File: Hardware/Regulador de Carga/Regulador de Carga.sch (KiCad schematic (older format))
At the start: 16 parts, among them K1 DIPxx-1Cxx-51x

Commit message: Regulador de carga
Modifique el circuito regulador de carga para hacerlo mas compacto y con menor consumo.
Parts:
- removed K1: DIPxx-1Cxx-51x, Relay_THT:Relay_SPDT_Finder_36.11, symbol Relay:DIPxx-1Cxx-51x
- removed ZENER1: D_Zener, Diode_THT:D_A-405_P12.70mm_Horizontal, symbol Device:D_Zener
- added D2: D_Zener, symbol Device:D_Zener
- added Q1: 2N3904, Package_TO_SOT_THT:TO-92_Inline, symbol Transistor_BJT:2N3904
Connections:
- wire segments 54 -> 49
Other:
- moved on the sheet: C3, D1, LED1, PANEL1, R2, RV1, op1

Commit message: Agregar huellas faltantes
le agregue las huellas que faltaban al regulador de carga
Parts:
- D2: footprint (none) -> Diode_THT:D_A-405_P12.70mm_Horizontal
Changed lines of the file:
@@
 F 0 "D2" H 3200 3317 50  0000 C CNN
 F 1 "D_Zener" H 3200 3226 50  0000 C CNN
-F 2 "" H 3200 3100 50  0001 C CNN
+F 2 "Diode_THT:D_A-405_P12.70mm_Horizontal" H 3200 3100 50  0001 C CNN
 F 3 "~" H 3200 3100 50  0001 C CNN
 	1    3200 3100

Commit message: regulador de carga (yeti)
es mi primer placa despues de años. ¿esta fachera, no?
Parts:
- added R4: 1K, Resistor_THT:R_Axial_DIN0204_L3.6mm_D1.6mm_P7.62mm_Horizontal, symbol Device:R
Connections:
- net at D2.2 (A): now also R4.1; no longer Q1.2 (B)
- new net: Q1.2 (B), R4.2
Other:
- moved on the sheet: BATin1, BATout1, C1, C2, C3, D1, D2, LED1, LM7805, PANEL1, Q1, R1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

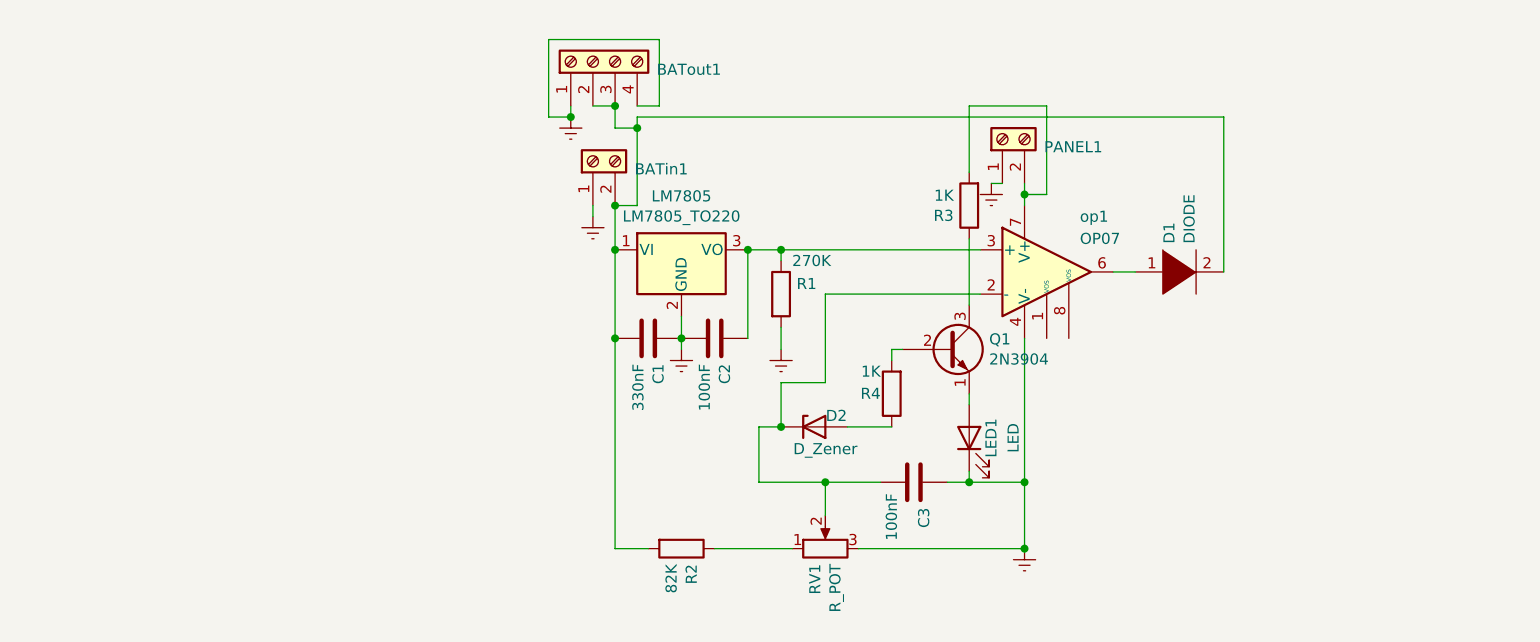
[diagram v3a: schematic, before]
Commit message: Esquematico Regulador de Carga
Agregue los 4 diodos en el esquematico.
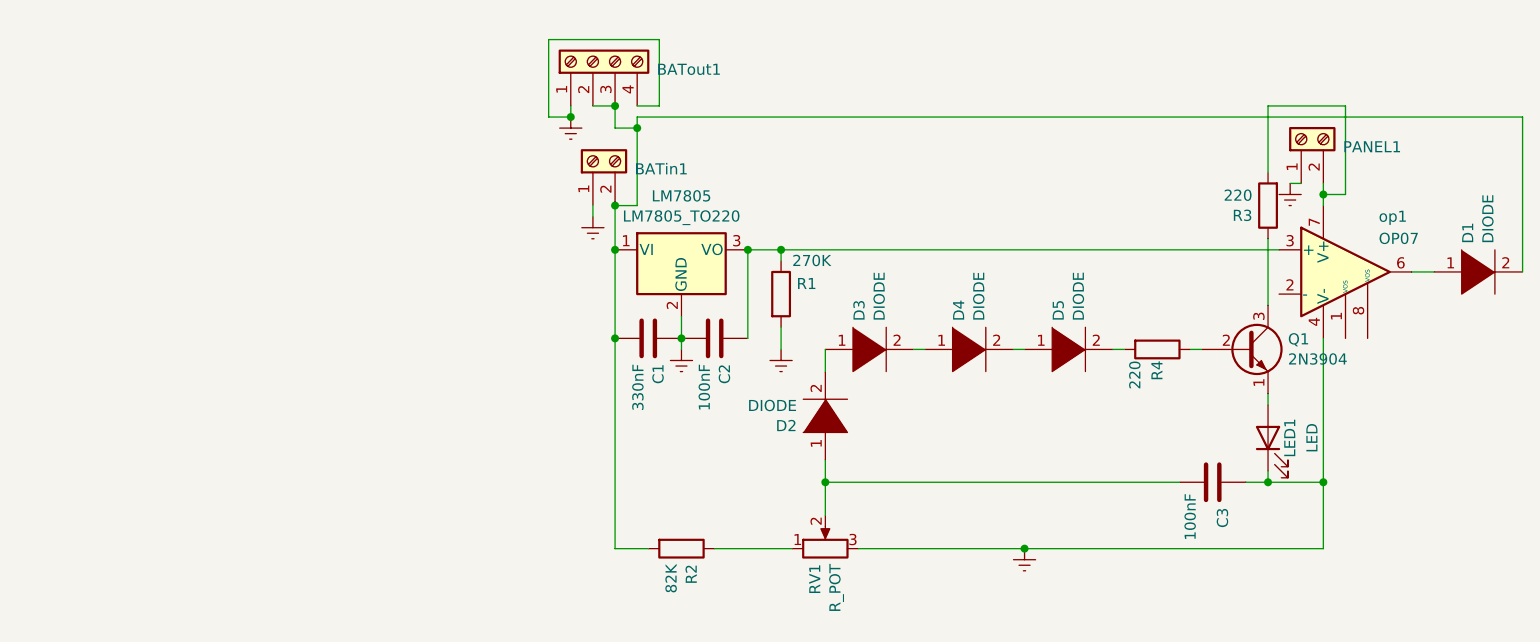
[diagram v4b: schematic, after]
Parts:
- removed D2: D_Zener, Diode_THT:D_A-405_P12.70mm_Horizontal, symbol Device:D_Zener
- added D2, D3, D4, D5: DIODE, Diode_THT:D_A-405_P12.70mm_Horizontal, symbol pspice:DIODE
- R3, R4: value 1K -> 220
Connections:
- net at C3.2, RV1.2: now also D2.1 (K); no longer op1.2 (-)
- net at R4.1: now also Q1.2 (B)
- net at R4.2: now also D5.2 (A); no longer Q1.2 (B)
- new net: D4.2 (A), D5.1 (K)
- new net: D3.2 (A), D4.1 (K)
- new net: D2.2 (A), D3.1 (K)
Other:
- moved on the sheet: C3, D1, LED1, PANEL1, Q1, R3, R4, op1
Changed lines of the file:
@@
 EESchema Schematic File Version 4
-LIBS:Regulador de Carga-cache
-EELAYER 29 0
+EELAYER 30 0
 EELAYER END
 $Descr A4 11693 8268
@@
 L Amplifier_Operational:OP07 op1
 U 1 1 5E9EA082
-P 6450 2850
-F 0 "op1" H 6600 3100 50  0000 L CNN
-F 1 "OP07" H 6600 3000 50  0000 L CNN
-F 2 "Package_DIP:DIP-8_W7.62mm" H 6500 2900 50  0001 C CNN
-F 3 "https://www.analog.com/media/en/technical-documentation/data-sheets/OP07.pdf" H 6500 3000 50  0001 C CNN
-	1    6450 2850
+P 7800 2850
+F 0 "op1" H 7950 3100 50  0000 L CNN
+F 1 "OP07" H 7950 3000 50  0000 L CNN
+F 2 "Package_DIP:DIP-8_W7.62mm" H 7850 2900 50  0001 C CNN
+F 3 "https://www.analog.com/media/en/technical-documentation/data-sheets/OP07.pdf" H 7850 3000 50  0001 C CNN
+	1    7800 2850
 	1    0    0    -1
 $EndComp
@@
 L Device:LED LED1
 U 1 1 5E9EAEE0
-P 6100 3600
-F 0 "LED1" H 6100 3500 50  0000 C CNN
-F 1 "LED" H 6100 3400 50  0000 C CNN
-F 2 "LED_THT:LED_D5.0mm" H 6100 3600 50  0001 C CNN
-F 3 "~" H 6100 3600 50  0001 C CNN
-	1    6100 3600
+P 7450 3600
+F 0 "LED1" H 7450 3500 50  0000 C CNN
+F 1 "LED" H 7450 3400 50  0000 C CNN
+F 2 "LED_THT:LED_D5.0mm" H 7450 3600 50  0001 C CNN
+F 3 "~" H 7450 3600 50  0001 C CNN
+	1    7450 3600
 	0    -1   -1   0
 $EndComp
@@
 L pspice:DIODE D1
 U 1 1 5E9E51EC
-P 7050 2850
-F 0 "D1" V 7004 2978 50  0000 L CNN
-F 1 "DIODE" V 7095 2978 50  0000 L CNN
-F 2 "Diode_THT:D_A-405_P12.70mm_Horizontal" H 7050 2850 50  0001 C CNN
-F 3 "~" H 7050 2850 50  0001 C CNN
-	1    7050 2850
+P 8400 2850
+F 0 "D1" V 8354 2978 50  0000 L CNN
+F 1 "DIODE" V 8445 2978 50  0000 L CNN
+F 2 "Diode_THT:D_A-405_P12.70mm_Horizontal" H 8400 2850 50  0001 C CNN
+F 3 "~" H 8400 2850 50  0001 C CNN
+	1    8400 2850
 	1    0    0    -1
 $EndComp
@@
 Wire Wire Line
 	5250 3100 5250 3200
-Connection ~ 5250 2750
 $Comp
 L Device:C C3
 U 1 1 5E9EDB4A
-P 5850 3800
-F 0 "C3" H 5965 3846 50  0000 L CNN
-F 1 "100nF" H 5900 3700 50  0000 L CNN
-F 2 "Capacitor_THT:C_Disc_D4.3mm_W1.9mm_P5.00mm" H 5888 3650 50  0001 C CNN
-F 3 "~" H 5850 3800 50  0001 C CNN
-	1    5850 3800
+P 7200 3800
+F 0 "C3" H 7315 3846 50  0000 L CNN
+F 1 "100nF" H 7250 3700 50  0000 L CNN
+F 2 "Capacitor_THT:C_Disc_D4.3mm_W1.9mm_P5.00mm" H 7238 3650 50  0001 C CNN
+F 3 "~" H 7200 3800 50  0001 C CNN
+	1    7200 3800
 	0    1    1    0
 $EndComp
@@
 L Connector:Screw_Terminal_01x02 PANEL1
 U 1 1 5E9F9816
-P 6250 2250
-F 0 "PANEL1" V 6214 2062 50  0000 R CNN
-F 1 "Screw_Terminal_01x02" V 6200 3200 50  0001 R CNN
-F 2 "TerminalBlock:TerminalBlock_bornier-2_P5.08mm" H 6250 2250 50  0001 C CNN
-F 3 "~" H 6250 2250 50  0001 C CNN
-	1    6250 2250
+P 7600 2250
+F 0 "PANEL1" V 7564 2062 50  0000 R CNN
+F 1 "Screw_Terminal_01x02" V 7550 3200 50  0001 R CNN
+F 2 "TerminalBlock:TerminalBlock_bornier-2_P5.08mm" H 7600 2250 50  0001 C CNN
+F 3 "~" H 7600 2250 50  0001 C CNN
+	1    7600 2250
 	0    -1   -1   0
 $EndComp
@@
 L power:Earth #PWR0107
 U 1 1 5E9FBB4D
-P 6200 2450
-F 0 "#PWR0107" H 6200 2200 50  0001 C CNN
-F 1 "Earth" H 6200 2300 50  0001 C CNN
-F 2 "" H 6200 2450 50  0001 C CNN
-F 3 "~" H 6200 2450 50  0001 C CNN
-	1    6200 2450
-	1    0    0    -1
-$EndComp
-Wire Wire Line
-	6250 2450 6200 2450
+P 7550 2450
+F 0 "#PWR0107" H 7550 2200 50  0001 C CNN
+F 1 "Earth" H 7550 2300 50  0001 C CNN
+F 2 "" H 7550 2450 50  0001 C CNN
+F 3 "~" H 7550 2450 50  0001 C CNN
+	1    7550 2450
+	1    0    0    -1
+$EndComp
+Wire Wire Line
+	7600 2450 7550 2450
 Wire Wire Line
 	4500 2100 4500 2200
@@
 Connection ~ 4500 2100
 Connection ~ 4500 2550
-$Comp
-L Device:D_Zener D2
-U 1 1 5EBDD3B2
-P 5400 3550
-F 0 "D2" H 5500 3600 50  0000 C CNN
-F 1 "D_Zener" H 5450 3450 50  0000 C CNN
-F 2 "Diode_THT:D_A-405_P12.70mm_Horizontal" H 5400 3550 50  0001 C CNN
-F 3 "~" H 5400 3550 50  0001 C CNN
-	1    5400 3550
-	1    0    0    -1
-$EndComp
-Wire Wire Line
-	6750 2850 6850 2850
-Wire Wire Line
-	7250 2850 7250 2150
+Wire Wire Line
+	8100 2850 8200 2850
+Wire Wire Line
+	8600 2850 8600 2150
 Wire Wire Line
 	4600 2150 4600 2200
@@
 L Transistor_BJT:2N3904 Q1
 U 1 1 5EBEE765
-P 6000 3200
-F 0 "Q1" H 6190 3246 50  0000 L CNN
-F 1 "2N3904" H 6190 3155 50  0000 L CNN
-F 2 "Package_TO_SOT_THT:TO-92_Inline" H 6200 3125 50  0001 L CIN
-F 3 "https://www.fairchildsemi.com/datasheets/2N/2N3904.pdf" H 6000 3200 50  0001 L CNN
-	1    6000 3200
+P 7350 3200
+F 0 "Q1" H 7540 3246 50  0000 L CNN
+F 1 "2N3904" H 7540 3155 50  0000 L CNN
+F 2 "Package_TO_SOT_THT:TO-92_Inline" H 7550 3125 50  0001 L CIN
+F 3 "https://www.fairchildsemi.com/datasheets/2N/2N3904.pdf" H 7350 3200 50  0001 L CNN
+	1    7350 3200
 	1    0    0    -1
 $EndComp
@@
 L Device:R R3
 U 1 1 5EBF2660
-P 6100 2550
-F 0 "R3" H 6170 2596 50  0000 L CNN
-F 1 "1K" H 6170 2505 50  0000 L CNN
-F 2 "Resistor_THT:R_Axial_DIN0204_L3.6mm_D1.6mm_P7.62mm_Horizontal" V 6030 2550 50  0001 C CNN
-F 3 "~" H 6100 2550 50  0001 C CNN
-	1    6100 2550
+P 7450 2550
+F 0 "R3" H 7520 2596 50  0000 L CNN
+F 1 "220" H 7520 2505 50  0000 L CNN
+F 2 "Resistor_THT:R_Axial_DIN0204_L3.6mm_D1.6mm_P7.62mm_Horizontal" V 7380 2550 50  0001 C CNN
+F 3 "~" H 7450 2550 50  0001 C CNN
+	1    7450 2550
 	-1   0    0    1
 $EndComp
 Wire Wire Line
-	6350 2450 6350 2500
-Wire Wire Line
-	4600 2150 7250 2150
-Wire Wire Line
-	6350 2500 6450 2500
-Wire Wire Line
-	6450 2500 6450 2100
-Wire Wire Line
-	6450 2100 6100 2100
-Wire Wire Line
-	6100 2100 6100 2400
-Connection ~ 6350 2500
-Wire Wire Line
-	6350 2500 6350 2550
-Wire Wire Line
-	5250 2750 6150 2750
-Wire Wire Line
-	6100 2700 6100 3000
-Wire Wire Line
-	5450 2950 6150 2950
-Wire Wire Line
-	6100 3400 6100 3450
-Wire Wire Line
-	5800 3200 5750 3200
+	7700 2450 7700 2500
+Wire Wire Line
+	7700 2500 7800 2500
+Wire Wire Line
+	7800 2500 7800 2100
+Wire Wire Line
+	7800 2100 7450 2100
+Wire Wire Line
+	7450 2100 7450 2400
+Connection ~ 7700 2500
+Wire Wire Line
+	7700 2500 7700 2550
+Wire Wire Line
+	7450 2700 7450 3000
+Wire Wire Line
+	7450 3400 7450 3450
 Wire Wire Line
 	4500 4100 4650 4100
@@
 	5600 4100 6350 4100
 Wire Wire Line
-	5700 3800 5450 3800
-Wire Wire Line
 	5450 3800 5450 3950
 Wire Wire Line
-	6000 3800 6100 3800
-Wire Wire Line
-	6100 3800 6100 3750
-Wire Wire Line
-	6350 3150 6350 3800
-Connection ~ 6350 4100
-Wire Wire Line
-	6100 3800 6350 3800
-Connection ~ 6100 3800
-Connection ~ 6350 3800
-Wire Wire Line
-	6350 3800 6350 4100
-Wire Wire Line
-	5450 3350 5450 2950
-Wire Wire Line
-	5150 3800 5450 3800
-Connection ~ 5450 3800
-Wire Wire Line
-	5150 3800 5150 3550
-Wire Wire Line
-	5150 3550 5250 3550
-Wire Wire Line
-	5250 3550 5250 3350
-Wire Wire Line
-	5250 3350 5450 3350
-Connection ~ 5250 3550
+	7350 3800 7450 3800
+Wire Wire Line
+	7450 3800 7450 3750
+Wire Wire Line
+	7700 3150 7700 3800
+Wire Wire Line
+	7450 3800 7700 3800
+Connection ~ 7450 3800
+Connection ~ 7700 3800
+Wire Wire Line
+	7700 3800 7700 4100
 $Comp
 L Device:R R4
 U 1 1 5EBEB6D4
-P 5750 3400
-F 0 "R4" H 5800 3400 50  0000 L CNN
-F 1 "1K" H 5800 3300 50  0000 L CNN
-F 2 "Resistor_THT:R_Axial_DIN0204_L3.6mm_D1.6mm_P7.62mm_Horizontal" V 5680 3400 50  0001 C CNN
-F 3 "~" H 5750 3400 50  0001 C CNN
-	1    5750 3400
-	-1   0    0    1
-$EndComp
-Wire Wire Line
-	5550 3550 5750 3550
-Wire Wire Line
-	5750 3250 5750 3200
+P 6950 3200
+F 0 "R4" H 7000 3200 50  0000 L CNN
+F 1 "220" H 7000 3100 50  0000 L CNN
+F 2 "Resistor_THT:R_Axial_DIN0204_L3.6mm_D1.6mm_P7.62mm_Horizontal" V 6880 3200 50  0001 C CNN
+F 3 "~" H 6950 3200 50  0001 C CNN
+	1    6950 3200
+	0    1    1    0
+$EndComp
+$Comp
+L pspice:DIODE D5
+U 1 1 5ECF23A4
+P 6550 3200
+F 0 "D5" V 6504 3328 50  0000 L CNN
+F 1 "DIODE" V 6595 3328 50  0000 L CNN
+F 2 "Diode_THT:D_A-405_P12.70mm_Horizontal" H 6550 3200 50  0001 C CNN
+F 3 "~" H 6550 3200 50  0001 C CNN
+	1    6550 3200
+	1    0    0    -1
+$EndComp
+$Comp
+L pspice:DIODE D4
+U 1 1 5ECFBDFE
+P 6100 3200
+F 0 "D4" V 6054 3328 50  0000 L CNN
+F 1 "DIODE" V 6145 3328 50  0000 L CNN
+F 2 "Diode_THT:D_A-405_P12.70mm_Horizontal" H 6100 3200 50  0001 C CNN
+F 3 "~" H 6100 3200 50  0001 C CNN
+	1    6100 3200
+	1    0    0    -1
+$EndComp
+$Comp
+L pspice:DIODE D3
+U 1 1 5ECFC15C
+P 5650 3200
+F 0 "D3" V 5604 3328 50  0000 L CNN
+F 1 "DIODE" V 5695 3328 50  0000 L CNN
+F 2 "Diode_THT:D_A-405_P12.70mm_Horizontal" H 5650 3200 50  0001 C CNN
+F 3 "~" H 5650 3200 50  0001 C CNN
+	1    5650 3200
+	1    0    0    -1
+$EndComp
+$Comp
+L pspice:DIODE D2
+U 1 1 5ECFE728
+P 5450 3500
+F 0 "D2" V 5404 3628 50  0000 L CNN
+F 1 "DIODE" V 5495 3628 50  0000 L CNN
+F 2 "Diode_THT:D_A-405_P12.70mm_Horizontal" H 5450 3500 50  0001 C CNN
+F 3 "~" H 5450 3500 50  0001 C CNN
+	1    5450 3500
+	0    -1   -1   0
+$EndComp
+Wire Wire Line
+	5450 3800 7050 3800
+Wire Wire Line
+	5450 3800 5450 3700
+Connection ~ 5450 3800
+Wire Wire Line
+	5450 3300 5450 3200
+Wire Wire Line
+	5250 2750 7500 2750
+Connection ~ 5250 2750
+Wire Wire Line
+	4600 2150 8600 2150
+Wire Wire Line
+	7700 4100 6350 4100
+Connection ~ 6350 4100
+Wire Wire Line
+	5850 3200 5900 3200
+Wire Wire Line
+	6300 3200 6350 3200
+Wire Wire Line
+	6750 3200 6800 3200
+Wire Wire Line
+	7100 3200 7150 3200
 $EndSCHEMATC
